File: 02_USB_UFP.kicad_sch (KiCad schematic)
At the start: 5 parts, among them J2 USB_C_Receptacle, U2 PI3USB302-Ax, U3 TUSB522Px

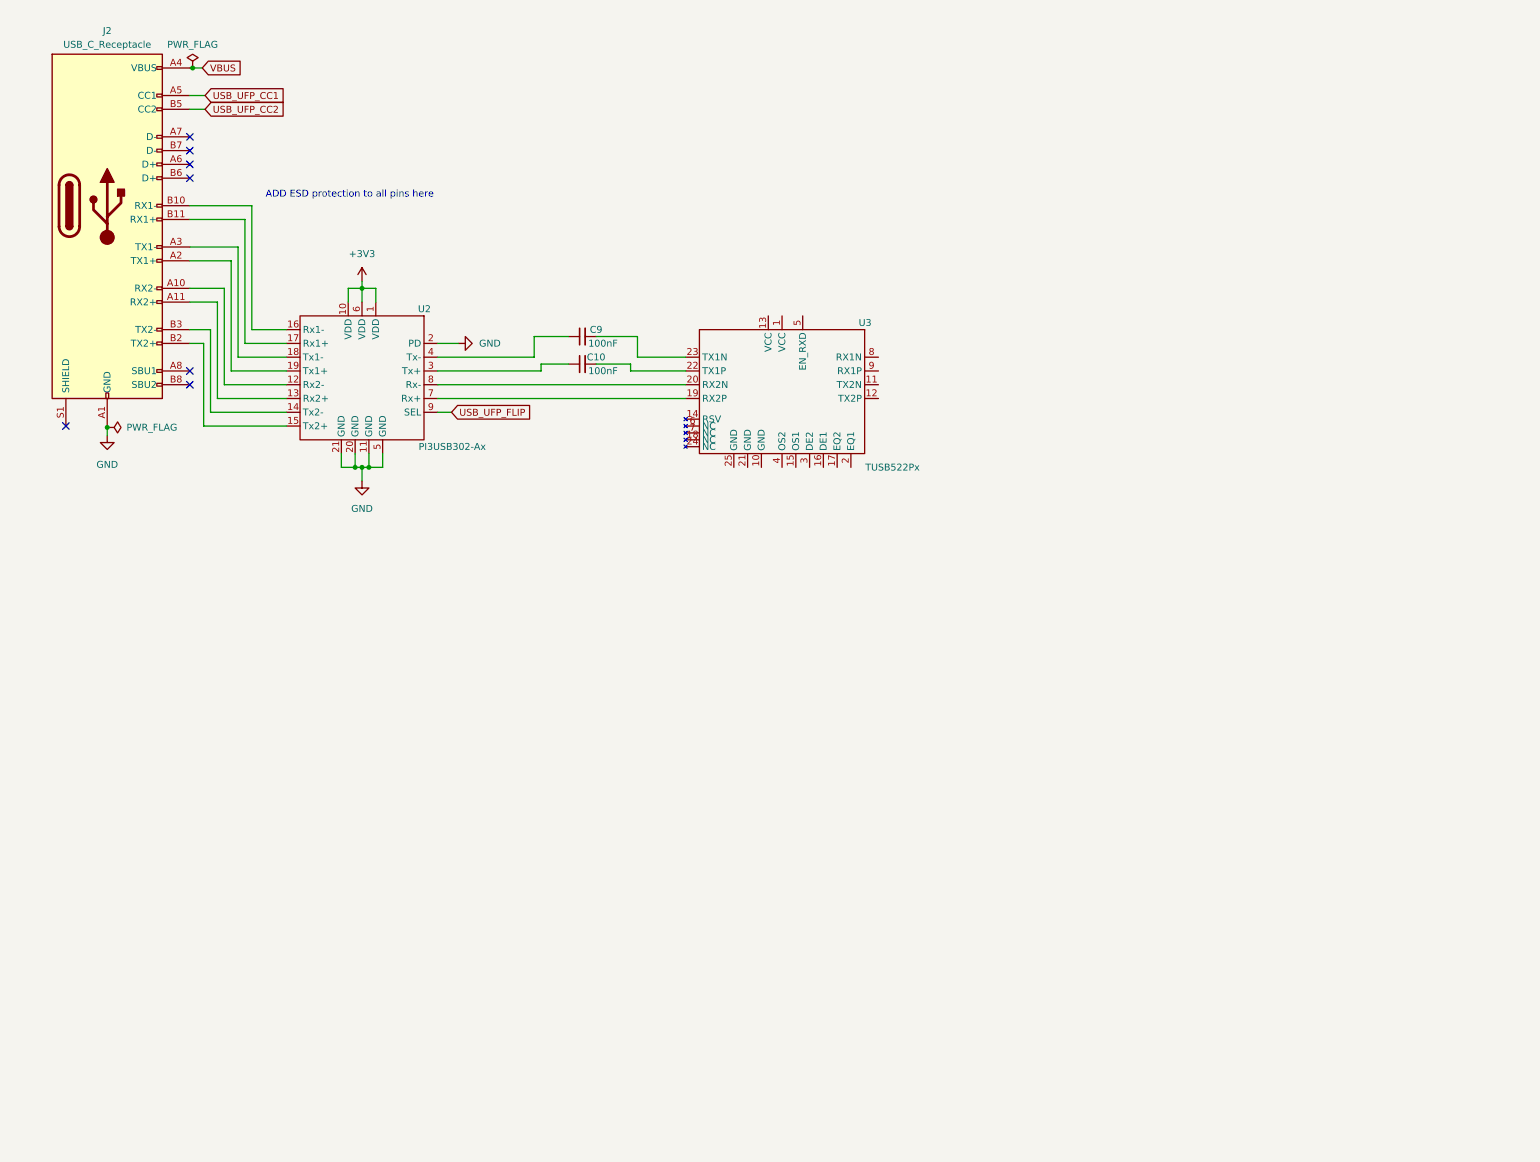
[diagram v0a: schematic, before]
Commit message: Add ESD protection for UFP, create buck converter model
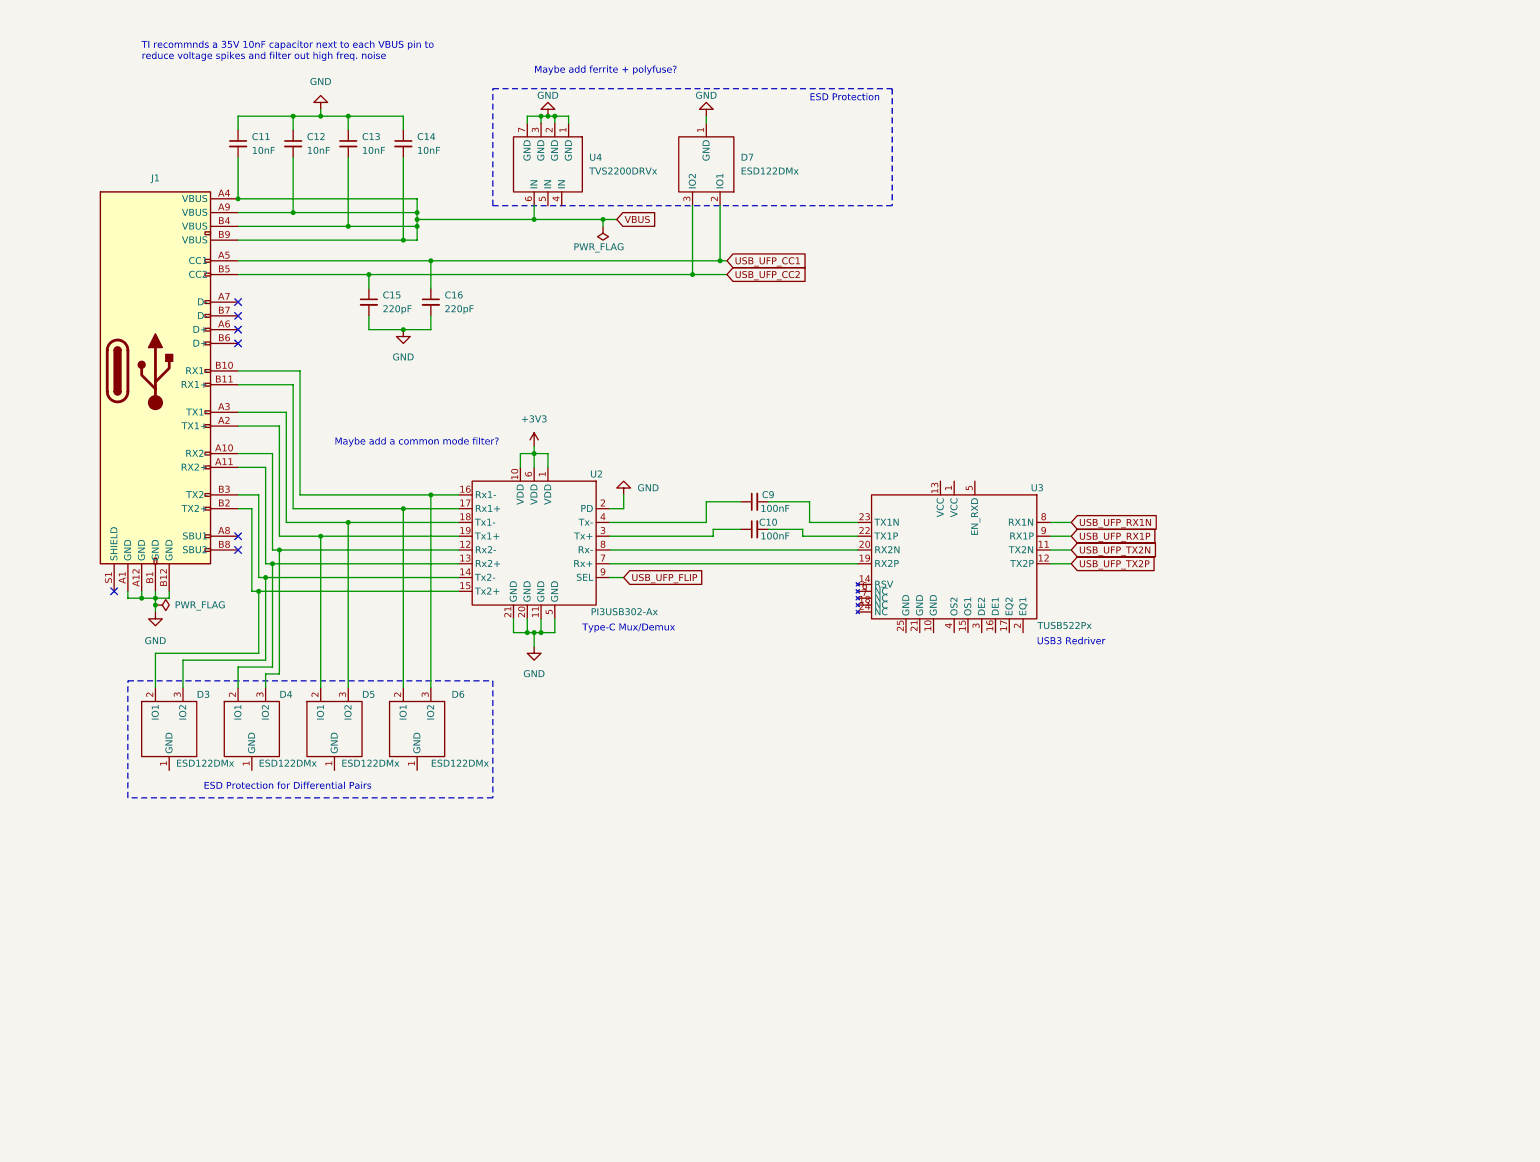
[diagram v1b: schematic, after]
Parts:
- removed J2: USB_C_Receptacle, Cake_USB:USB_C_Receptacle_GT-USB-7052, symbol Connector:USB_C_Receptacle
- added C11, C12, C13, C14: 10nF, symbol Device:C_Small
- added C15, C16: 220pF, symbol Device:C_Small
- added D3, D4, D5, D6, D7: ESD122DMx, Cake_USB:ESD122DMX, symbol CakeUSB:ESD122DMx
- added J1: ~, symbol CakeUSB:USB_C_Receptacle
- added U4: TVS2200DRVx, symbol CakeUSB:TVS2200DRVx
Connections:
- net GND: now also C11.1, C12.1, C13.1, C14.1, C15.2, C16.2, D7.1 (GND), J1.A1 (GND), J1.A12 (GND), J1.B1 (GND), J1.B12 (GND), U4.1 (GND), U4.2 (GND), U4.3 (GND), U4.7 (GND)
- net USB_UFP_CC1: now also C16.1, D7.2 (IO1), J1.A5 (CC1)
- net USB_UFP_CC2: now also C15.1, D7.3 (IO2), J1.B5 (CC2)
- net VBUS: now also C11.2, C12.2, C13.2, C14.2, J1.A4 (VBUS), J1.A9 (VBUS), J1.B4 (VBUS), J1.B9 (VBUS), U4.6 (IN)
- net at U2.12 (Rx2-): now also D4.3 (IO2), J1.A10 (RX2-)
- net at U2.13 (Rx2+): now also D4.2 (IO1), J1.A11 (RX2+)
- net at U2.19 (Tx1+): now also D5.2 (IO1), J1.A2 (TX1+)
- net at U2.18 (Tx1-): now also D5.3 (IO2), J1.A3 (TX1-)
- net at U2.16 (Rx1-): now also D6.3 (IO2), J1.B10 (RX1-)
- net at U2.17 (Rx1+): now also D6.2 (IO1), J1.B11 (RX1+)
- net at U2.15 (Tx2+): now also D3.2 (IO1), J1.B2 (TX2+)
- net at U2.14 (Tx2-): now also D3.3 (IO2), J1.B3 (TX2-)
- net USB_UFP_TX2N: now reaches U3.11 (TX2N)
- net USB_UFP_TX2P: now reaches U3.12 (TX2P)
- net USB_UFP_RX1N: now reaches U3.8 (RX1N)
- net USB_UFP_RX1P: now reaches U3.9 (RX1P)
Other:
- note added: "ESD Protection"
- note added: "ESD Protection for Differential Pairs"
- note added: "Maybe add a common mode filter?"
- note added: "Maybe add ferrite + polyfuse?"
- note added: "TI recommnds a 35V 10nF capacitor next to each VBUS pin to reduce voltage spikes and filter out high freq. noise"
- note added: "Type-C Mux/Demux"
- note added: "USB3 Redriver"
- note removed: "ADD ESD protection to all pins here"
- moved on the sheet: C10, C9, U2, U3

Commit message: more work on the power section
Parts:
- U4: footprint (none) -> Cake_USB:TVS2200DRVx
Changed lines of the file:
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@@
     )
   )
-  (symbol (lib_id "CakeUSB:ESD122DMx") (at 72.39 144.78 0) (unit 1)
+  (symbol (lib_name "ESD122DMx_1") (lib_id "CakeUSB:ESD122DMx") (at 72.39 144.78 0) (unit 1)
     (in_bom yes) (on_board yes) (dnp no)
     (property "Reference" "D5" (at 77.47 138.43 0)
@@
     )
   )
-  (symbol (lib_id "CakeUSB:ESD122DMx") (at 41.91 144.78 0) (unit 1)
+  (symbol (lib_name "ESD122DMx_3") (lib_id "CakeUSB:ESD122DMx") (at 41.91 144.78 0) (unit 1)
     (in_bom yes) (on_board yes) (dnp no)
     (property "Reference" "D3" (at 46.99 138.43 0)
@@
       (effects (font (size 1.27 1.27)) (justify left))
     )
-    (property "Footprint" "" (at 111.76 40.64 0)
+    (property "Footprint" "Cake_USB:TVS2200DRVx" (at 111.76 40.64 0)
       (effects (font (size 1.27 1.27)) hide)
     )
@@
     )
   )
-  (symbol (lib_id "CakeUSB:ESD122DMx") (at 57.15 144.78 0) (unit 1)
+  (symbol (lib_name "ESD122DMx_2") (lib_id "CakeUSB:ESD122DMx") (at 57.15 144.78 0) (unit 1)
     (in_bom yes) (on_board yes) (dnp no)
     (property "Reference" "D4" (at 62.23 138.43 0)
@@
     )
   )
-  (symbol (lib_id "CakeUSB:ESD122DMx") (at 87.63 144.78 0) (unit 1)
+  (symbol (lib_name "ESD122DMx_4") (lib_id "CakeUSB:ESD122DMx") (at 87.63 144.78 0) (unit 1)
     (in_bom yes) (on_board yes) (dnp no)
     (property "Reference" "D6" (at 93.98 138.43 0)

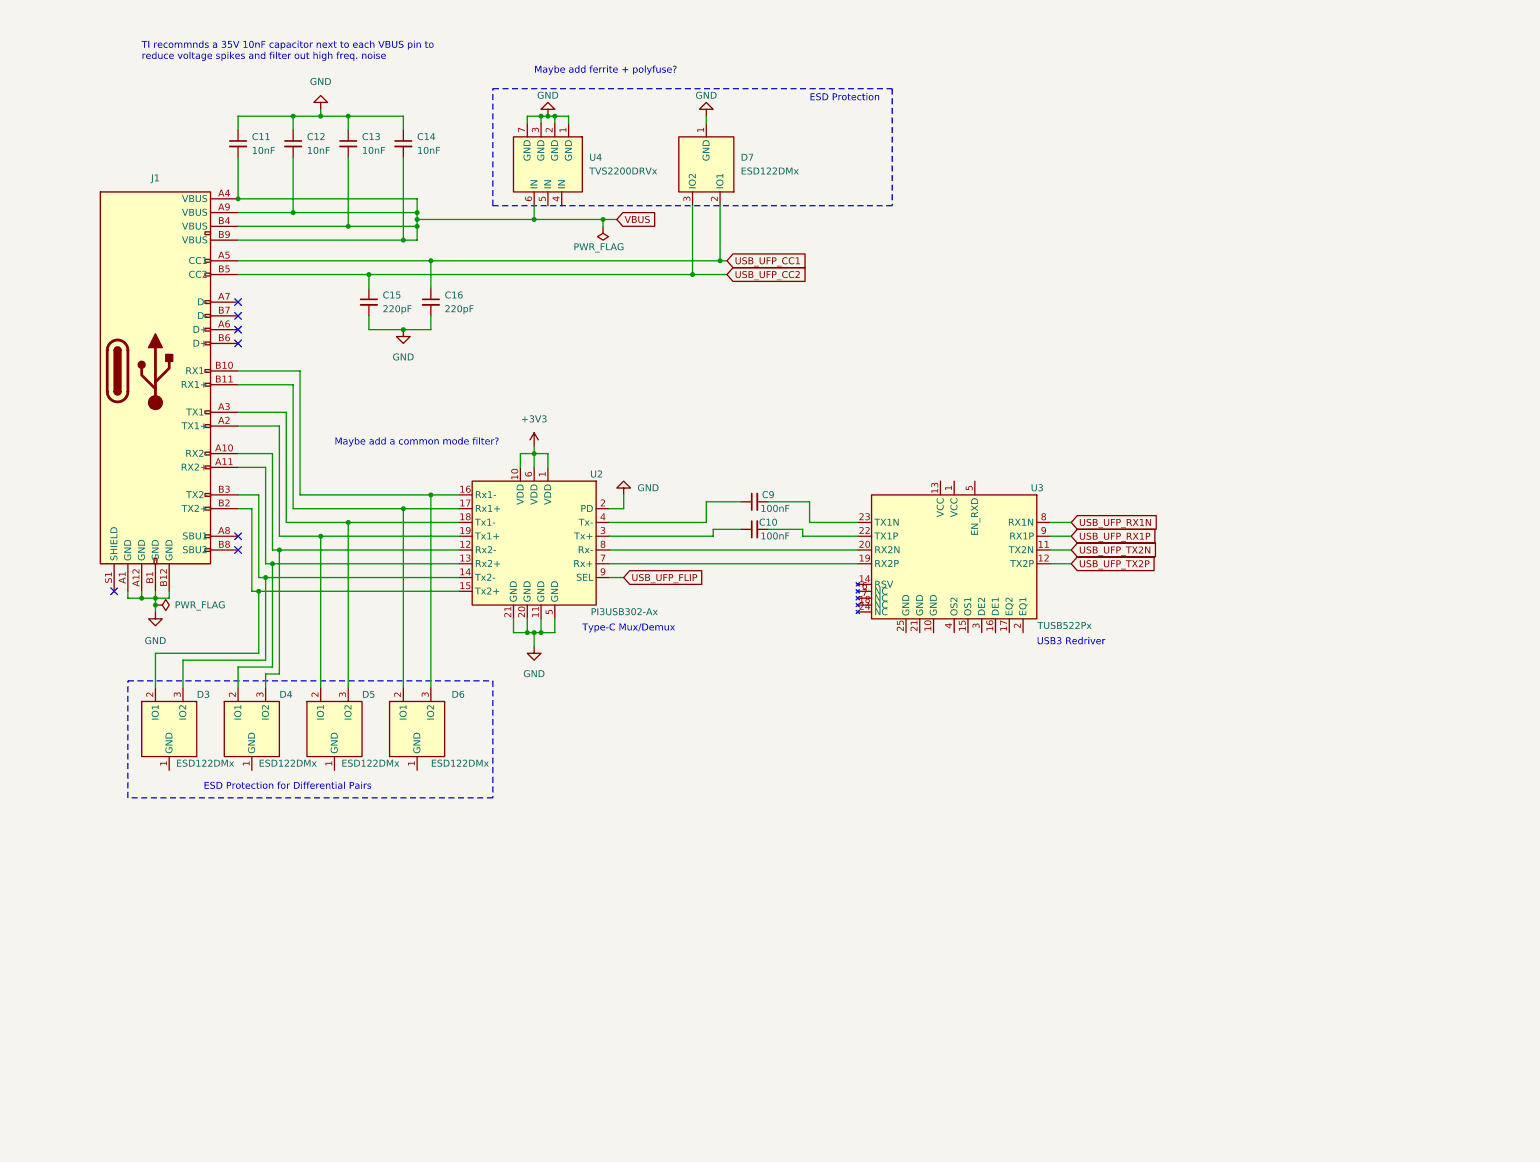
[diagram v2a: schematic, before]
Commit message: add usb hub controller schematic, fix up redriver
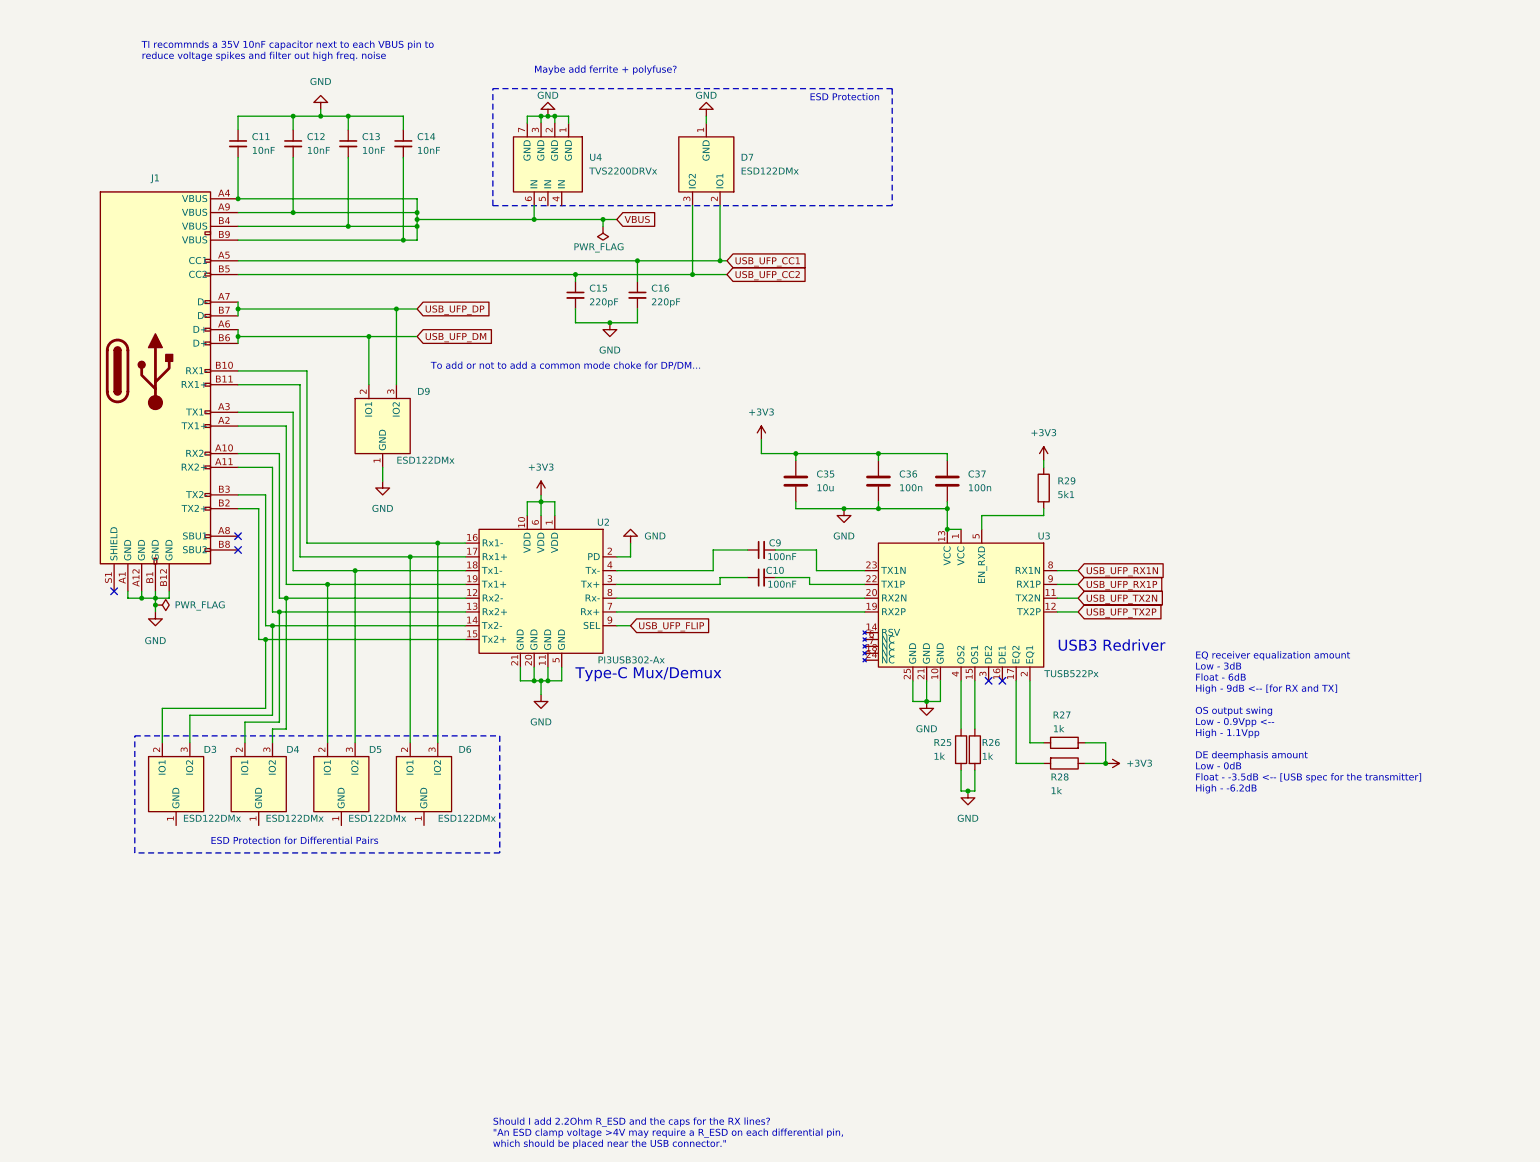
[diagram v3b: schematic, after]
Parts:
- added C35: 10u, symbol Device:C
- added C36, C37: 100n, symbol Device:C
- added D9: ESD122DMx, Cake_USB:ESD122DMX, symbol CakeUSB:ESD122DMx
- added R25, R26, R27, R28: 1k, symbol Device:R
- added R29: 5k1, symbol Device:R
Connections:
- net +3V3: now also C35.1, C36.1, C37.1, R27.2, R28.1, R29.1
- net GND: now also U3.1 (VCC), U3.10 (GND), U3.13 (VCC), U3.21 (GND), U3.25 (GND), C35.2, C36.2, C37.2, D9.1 (GND), R25.2, R26.2
- net at U3.15 (OS1): now also R26.1
- net at U3.17 (EQ2): now also R28.2
- net at U3.2 (EQ1): now also R27.1
- net at U3.4 (OS2): now also R25.1
- net at U3.5 (EN_RXD): now also R29.2
- net USB_UFP_DM: now reaches J1.A6 (D+)
- net USB_UFP_DM: now also J1.B6 (D+), D9.2 (IO1)
- net USB_UFP_DP: now reaches J1.A7 (D-)
- net USB_UFP_DP: now also J1.B7 (D-), D9.3 (IO2)
- no-connect marks 7 -> 5
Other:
- note added: "EQ receiver equalization amount Low - 3dB Float - 6dB High - 9dB <-- [for RX and TX] OS output swing Low - 0.9Vpp <-- High - 1.1Vpp DE deemphasis amount Low - 0dB Float - -3.5dB <-- [USB spec for the transmitter] High - -6.2dB"
- note added: "Should I add 2.2Ohm R_ESD and the caps for the RX lines? "An ESD clamp voltage >4V may require a R_ESD on each differential pin, which should be placed near the USB connector.""
- note added: "To add or not to add a common mode choke for DP/DM..."
- note removed: "Maybe add a common mode filter?"
- moved on the sheet: C10, C15, C16, C9, D3, D4, D5, D6, U2, U3

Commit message: WIP hub and DFP
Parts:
- added C93, C94, C95, C96: 100n, symbol Device:C_Small
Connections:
- net USB_UFP_RX1N: no longer names the net of U3.8 (RX1N)
- net USB_UFP_RX1N: now also C93.1
- net USB_UFP_RX1P: no longer names the net of U3.9 (RX1P)
- net USB_UFP_RX1P: now also C94.1
- net USB_UFP_TX2N: no longer names the net of U3.11 (TX2N)
- net USB_UFP_TX2N: now also C95.1
- net USB_UFP_TX2P: no longer names the net of U3.12 (TX2P)
- net USB_UFP_TX2P: now also C96.1
- new net USB_UFP_RXN: C95.2
- new net USB_UFP_RXP: C96.2
- new net USB_UFP_TXN: C93.2
- new net USB_UFP_TXP: C94.2
